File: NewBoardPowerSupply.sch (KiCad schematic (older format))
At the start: 22 parts, among them IC1 ADM7172ACPZ-4.2-R7, IC2 LT1716CS5#TRPBF, IC3 ADM7154ARDZ-3.3-R7, IC4 IRF9358PBF, U3 LM4040EIM3X-2.5_NOPB

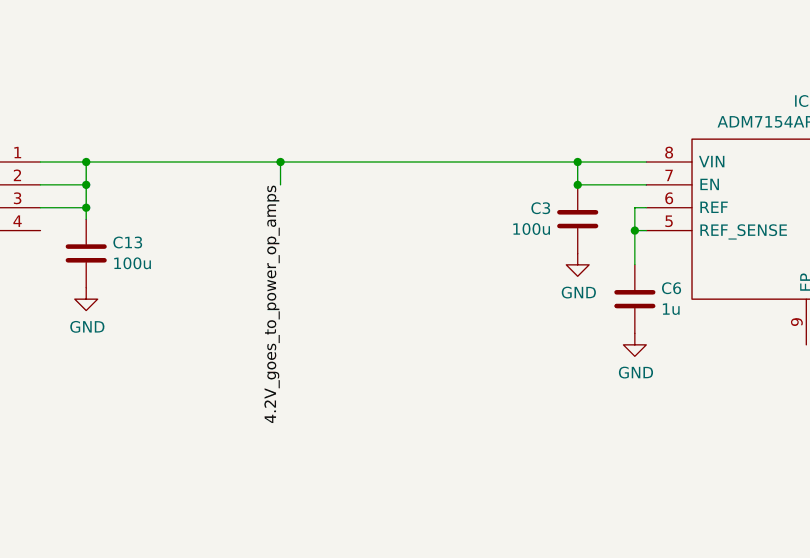
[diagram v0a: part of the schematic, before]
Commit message: added 4.2V port from pwr supply to pwr op amps sheet
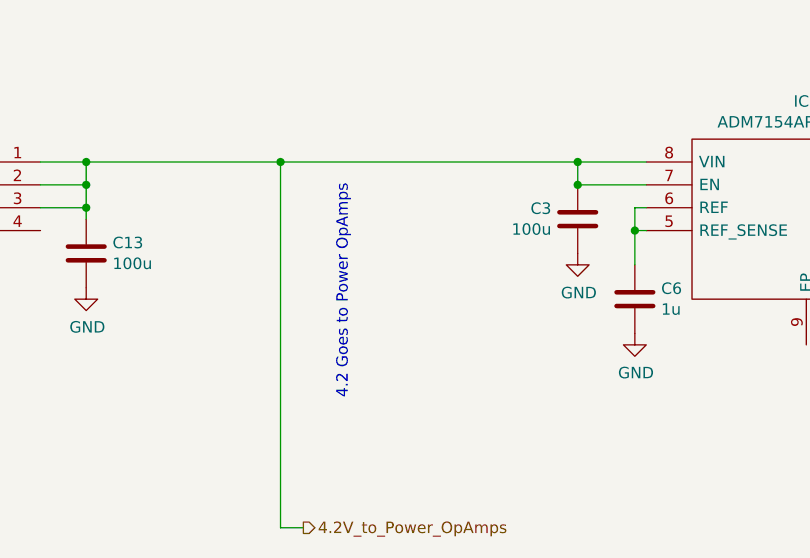
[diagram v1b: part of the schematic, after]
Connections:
- net 4.2V_goes_to_power_op_amps renamed 4.2V_to_Power_OpAmps
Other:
- note added: "4.2 Goes to Power OpAmps"
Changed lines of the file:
@@
 Text Label 8900 5500 0    50   ~ 0
 3.3V_rail
-Wire Wire Line
-	4650 5500 4650 5400
 Connection ~ 4650 5400
 Wire Wire Line
 	4650 5400 3800 5400
-Text Label 4650 5500 3    50   ~ 0
-4.2V_goes_to_power_op_amps
 Connection ~ 7600 2500
 Wire Wire Line
@@
 	7800 2100 7800 2500
 Connection ~ 6100 1000
+Text Notes 4950 5500 3    50   ~ 0
+4.2 Goes to Power OpAmps
+Text HLabel 4750 7000 2    50   Output ~ 0
+4.2V_to_Power_OpAmps
+Wire Wire Line
+	4650 7000 4750 7000
+Wire Wire Line
+	4650 5400 4650 7000
 $EndSCHEMATC

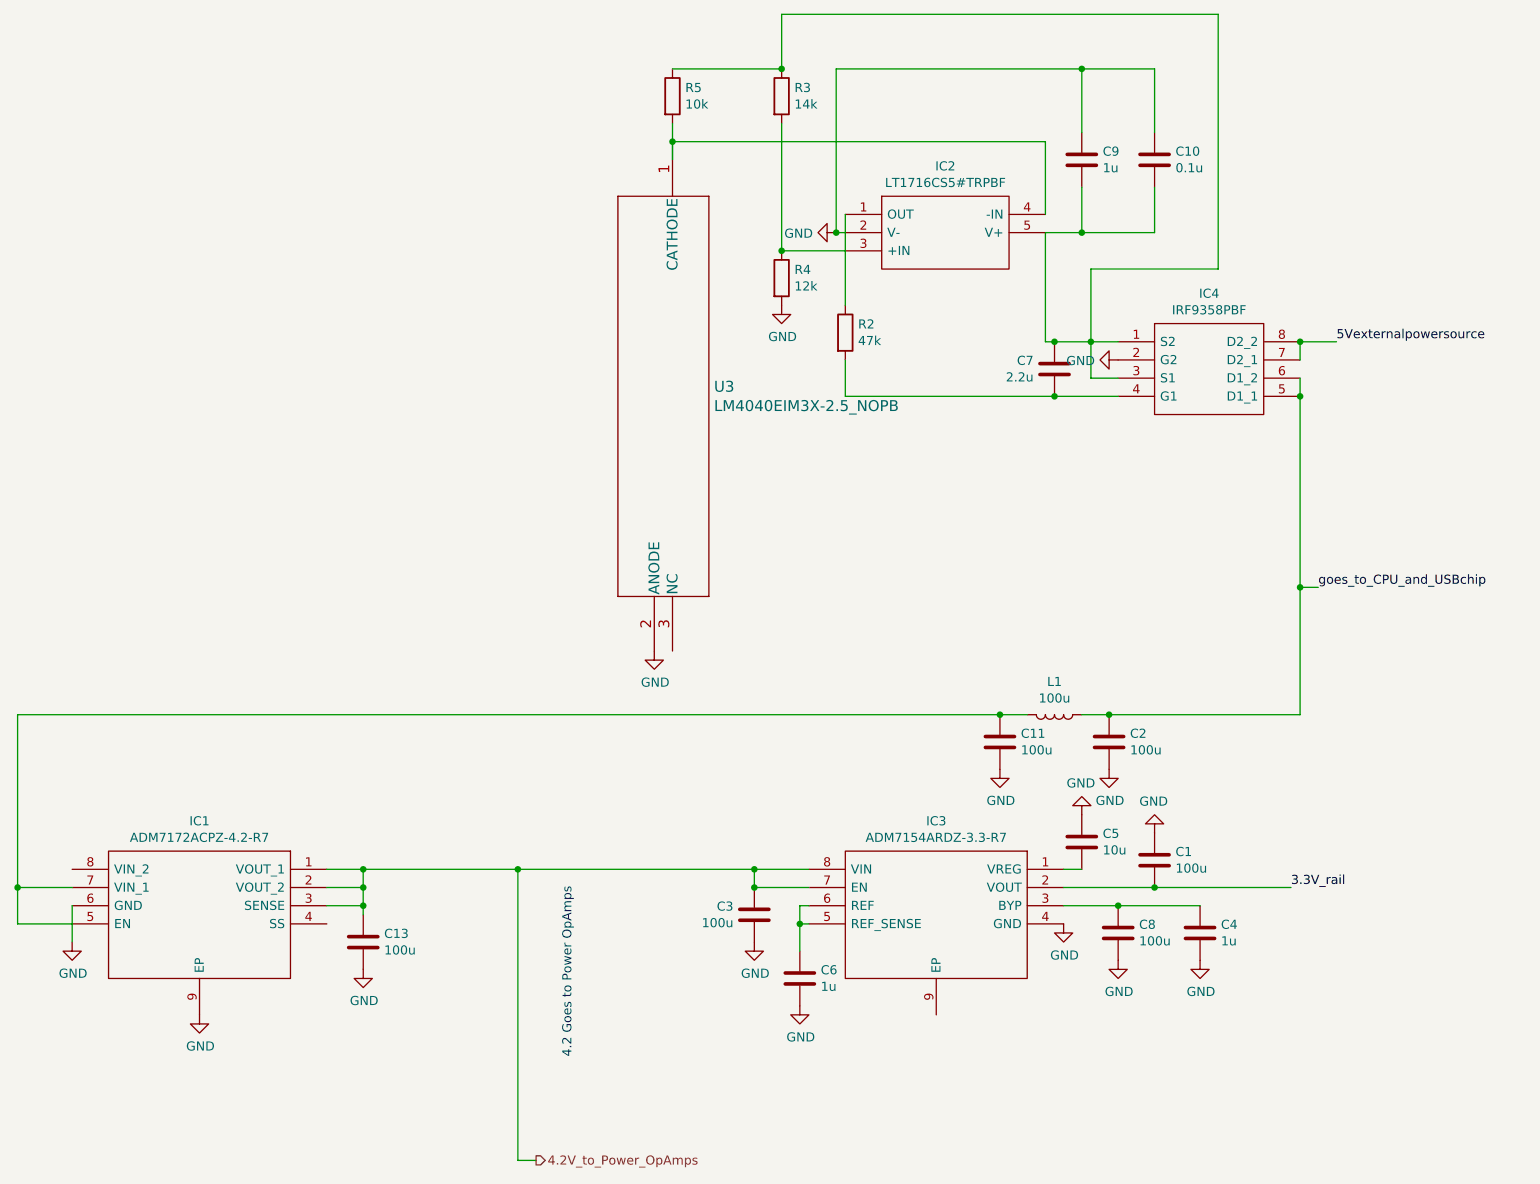
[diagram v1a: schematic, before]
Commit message: annotate all sheets
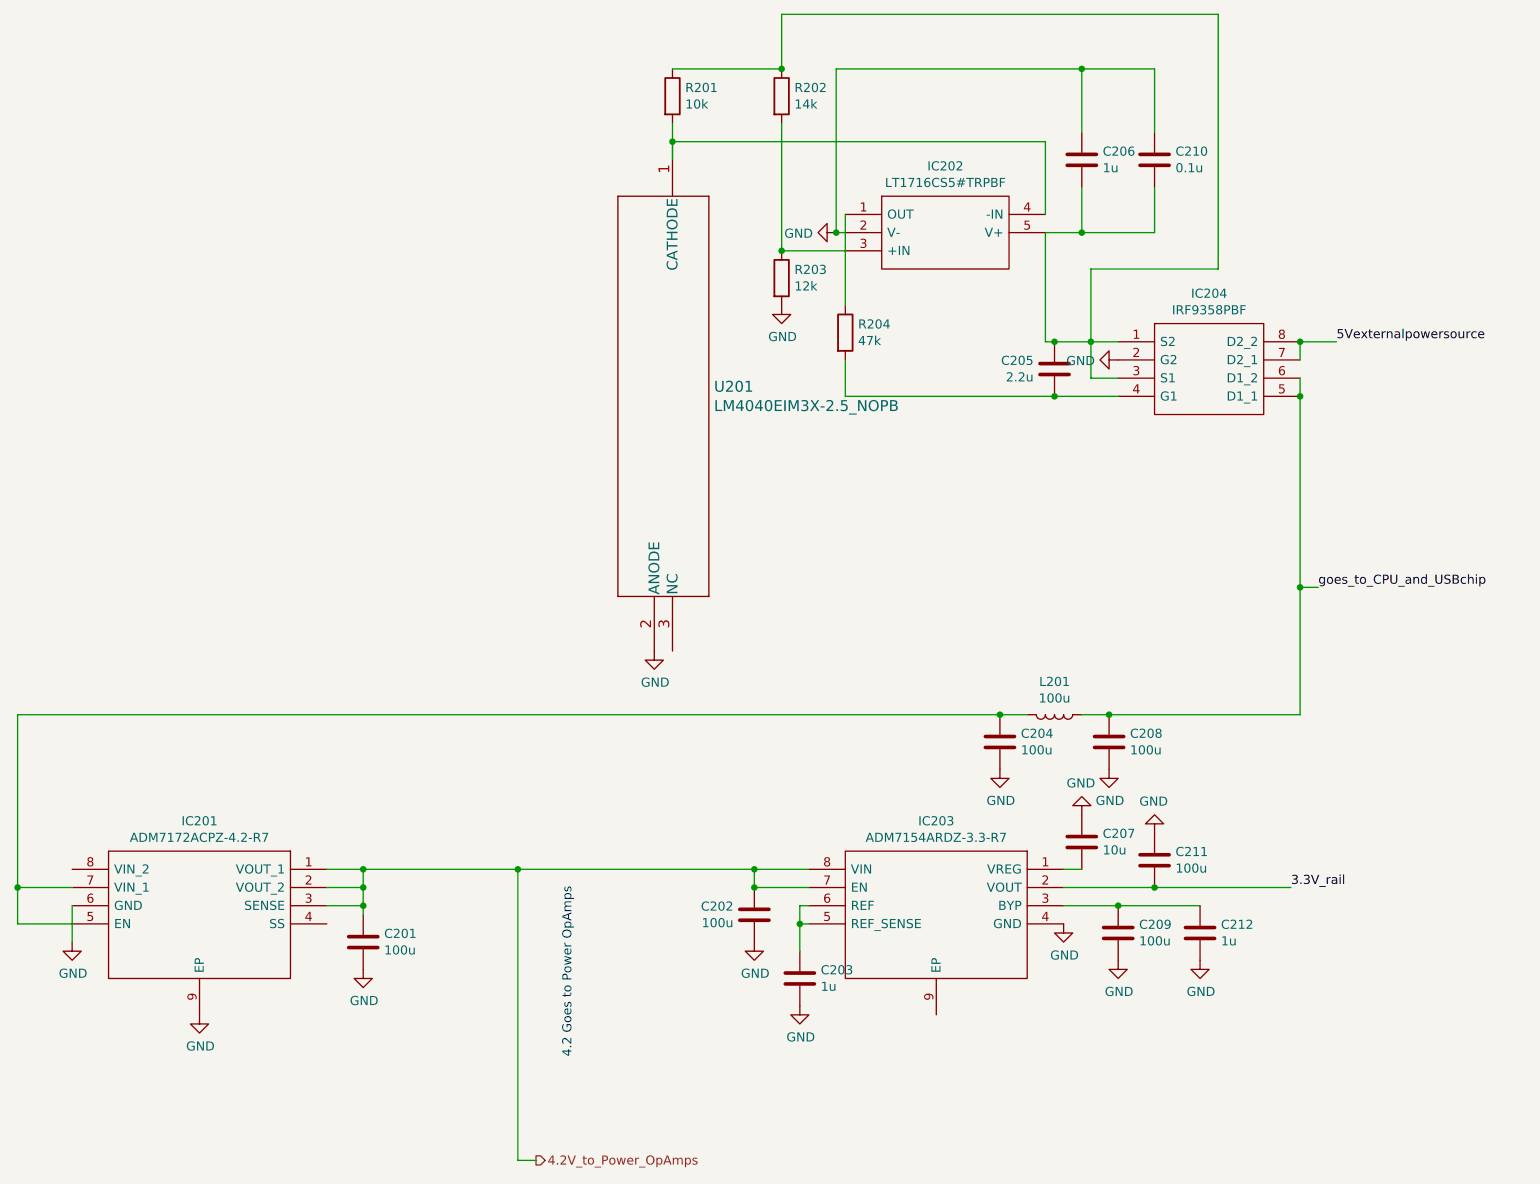
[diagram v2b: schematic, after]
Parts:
- renumbered C13 to C201, C3 to C202, C6 to C203, C11 to C204, C7 to C205, C9 to C206, C5 to C207, C2 to C208, C8 to C209, C10 to C210, C1 to C211, C4 to C212, IC1 to IC201, IC2 to IC202, IC3 to IC203, IC4 to IC204, L1 to L201, R5 to R201, R3 to R202, R4 to R203, R2 to R204, U3 to U201
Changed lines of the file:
@@
 $EndDescr
 $Comp
-L ADM7172ACPZ-4.2-R7:ADM7172ACPZ-4.2-R7 IC1
+L ADM7172ACPZ-4.2-R7:ADM7172ACPZ-4.2-R7 IC201
 U 1 1 60C1104B
 P 3600 5400
-F 0 "IC1" H 4300 5665 50  0000 C CNN
+F 0 "IC201" H 4300 5665 50  0000 C CNN
 F 1 "ADM7172ACPZ-4.2-R7" H 4300 5574 50  0000 C CNN
 F 2 "SON50P300X300X80-9N-D" H 4850 5500 50  0001 L CNN
@@
 $EndComp
 $Comp
-L Device:C C13
+L Device:C C201
 U 1 1 60C1975B
 P 3800 5800
-F 0 "C13" H 3915 5846 50  0000 L CNN
+F 0 "C201" H 3915 5846 50  0000 L CNN
 F 1 "100u" H 3915 5755 50  0000 L CNN
 F 2 "" H 3838 5650 50  0001 C CNN
@@
 $EndComp
 $Comp
-L power:GND #PWR01
+L power:GND #PWR0202
 U 1 1 60C1A400
 P 2900 6200
-F 0 "#PWR01" H 2900 5950 50  0001 C CNN
+F 0 "#PWR0202" H 2900 5950 50  0001 C CNN
 F 1 "GND" H 2905 6027 50  0000 C CNN
 F 2 "" H 2900 6200 50  0001 C CNN
@@
 $EndComp
 $Comp
-L power:GND #PWR02
+L power:GND #PWR0203
 U 1 1 60C1ADE2
 P 3800 5950
-F 0 "#PWR02" H 3800 5700 50  0001 C CNN
+F 0 "#PWR0203" H 3800 5700 50  0001 C CNN
 F 1 "GND" H 3805 5777 50  0000 C CNN
 F 2 "" H 3800 5950 50  0001 C CNN
@@
 $EndComp
 $Comp
-L ADM7154ARDZ-3.3-R7:ADM7154ARDZ-3.3-R7 IC3
+L ADM7154ARDZ-3.3-R7:ADM7154ARDZ-3.3-R7 IC203
 U 1 1 60C11888
 P 7650 5400
-F 0 "IC3" H 8350 5665 50  0000 C CNN
+F 0 "IC203" H 8350 5665 50  0000 C CNN
 F 1 "ADM7154ARDZ-3.3-R7" H 8350 5574 50  0000 C CNN
 F 2 "SOIC127P600X175-9N" H 8900 5500 50  0001 L CNN
@@
 $EndComp
 $Comp
-L Device:C C3
+L Device:C C202
 U 1 1 60C28A84
 P 5950 5650
-F 0 "C3" H 6065 5696 50  0000 L CNN
+F 0 "C202" H 6065 5696 50  0000 L CNN
 F 1 "100u" H 6065 5605 50  0000 L CNN
 F 2 "" H 5988 5500 50  0001 C CNN
@@
 $EndComp
 $Comp
-L Device:C C4
+L Device:C C212
 U 1 1 60C2CB1A
 P 8400 5750
-F 0 "C4" H 8515 5796 50  0000 L CNN
+F 0 "C212" H 8515 5796 50  0000 L CNN
 F 1 "1u" H 8515 5705 50  0000 L CNN
 F 2 "" H 8438 5600 50  0001 C CNN
@@
 $EndComp
 $Comp
-L Device:C C8
+L Device:C C209
 U 1 1 60C2E0AC
 P 7950 5750
-F 0 "C8" H 8065 5796 50  0000 L CNN
+F 0 "C209" H 8065 5796 50  0000 L CNN
 F 1 "100u" H 8065 5705 50  0000 L CNN
 F 2 "" H 7988 5600 50  0001 C CNN
@@
 $EndComp
 $Comp
-L power:GND #PWR015
+L power:GND #PWR0216
 U 1 1 60C305D6
 P 8400 5900
-F 0 "#PWR015" H 8400 5650 50  0001 C CNN
+F 0 "#PWR0216" H 8400 5650 50  0001 C CNN
 F 1 "GND" H 8405 5727 50  0000 C CNN
 F 2 "" H 8400 5900 50  0001 C CNN
@@
 $EndComp
 $Comp
-L power:GND #PWR013
+L power:GND #PWR0214
 U 1 1 60C30DEB
 P 7950 5900
-F 0 "#PWR013" H 7950 5650 50  0001 C CNN
+F 0 "#PWR0214" H 7950 5650 50  0001 C CNN
 F 1 "GND" H 7955 5727 50  0000 C CNN
 F 2 "" H 7950 5900 50  0001 C CNN
@@
 	6250 5500 5950 5500
 $Comp
-L power:GND #PWR04
+L power:GND #PWR0205
 U 1 1 60C319E0
 P 5950 5800
-F 0 "#PWR04" H 5950 5550 50  0001 C CNN
+F 0 "#PWR0205" H 5950 5550 50  0001 C CNN
 F 1 "GND" H 5955 5627 50  0000 C CNN
 F 2 "" H 5950 5800 50  0001 C CNN
@@
 $EndComp
 $Comp
-L Device:C C5
+L Device:C C207
 U 1 1 60C31F44
 P 7750 5250
-F 0 "C5" H 7865 5296 50  0000 L CNN
+F 0 "C207" H 7865 5296 50  0000 L CNN
 F 1 "10u" H 7865 5205 50  0000 L CNN
 F 2 "" H 7788 5100 50  0001 C CNN
@@
 	7650 5400 7750 5400
 $Comp
-L power:GND #PWR010
+L power:GND #PWR0211
 U 1 1 60C366F1
 P 7750 5100
-F 0 "#PWR010" H 7750 4850 50  0001 C CNN
+F 0 "#PWR0211" H 7750 4850 50  0001 C CNN
 F 1 "GND" H 7755 4927 50  0000 C CNN
 F 2 "" H 7750 5100 50  0001 C CNN
@@
 Connection ~ 5950 5500
 $Comp
-L Device:C C6
+L Device:C C203
 U 1 1 60C3804B
 P 6200 6000
-F 0 "C6" H 6315 6046 50  0000 L CNN
+F 0 "C203" H 6315 6046 50  0000 L CNN
 F 1 "1u" H 6315 5955 50  0000 L CNN
 F 2 "" H 6238 5850 50  0001 C CNN
@@
 	6200 5700 6200 5850
 $Comp
-L power:GND #PWR06
+L power:GND #PWR0207
 U 1 1 60C392F3
 P 6200 6150
-F 0 "#PWR06" H 6200 5900 50  0001 C CNN
+F 0 "#PWR0207" H 6200 5900 50  0001 C CNN
 F 1 "GND" H 6205 5977 50  0000 C CNN
 F 2 "" H 6200 6150 50  0001 C CNN
@@
 $EndComp
 $Comp
-L Device:C C1
+L Device:C C211
 U 1 1 60C39B45
 P 8150 5350
-F 0 "C1" H 8265 5396 50  0000 L CNN
+F 0 "C211" H 8265 5396 50  0000 L CNN
 F 1 "100u" H 8265 5305 50  0000 L CNN
 F 2 "" H 8188 5200 50  0001 C CNN
@@
 	7650 5500 8150 5500
 $Comp
-L power:GND #PWR014
+L power:GND #PWR0215
 U 1 1 60C3BD4C
 P 8150 5200
-F 0 "#PWR014" H 8150 4950 50  0001 C CNN
+F 0 "#PWR0215" H 8150 4950 50  0001 C CNN
 F 1 "GND" H 8155 5027 50  0000 C CNN
 F 2 "" H 8150 5200 50  0001 C CNN
@@
 	1900 5500 2200 5500
 $Comp
-L Device:C C11
+L Device:C C204
 U 1 1 60C3DCA3
 P 7300 4700
-F 0 "C11" H 7185 4654 50  0000 R CNN
+F 0 "C204" H 7185 4654 50  0000 R CNN
 F 1 "100u" H 7185 4745 50  0000 R CNN
 F 2 "" H 7338 4550 50  0001 C CNN
@@
 $EndComp
 $Comp
-L Device:L L1
+L Device:L L201
 U 1 1 60C3F9A3
 P 7600 4550
-F 0 "L1" V 7419 4550 50  0000 C CNN
+F 0 "L201" V 7419 4550 50  0000 C CNN
 F 1 "100u" V 7510 4550 50  0000 C CNN
 F 2 "" H 7600 4550 50  0001 C CNN
@@
 $EndComp
 $Comp
-L power:GND #PWR08
+L power:GND #PWR0209
 U 1 1 60C42E03
 P 7300 4850
-F 0 "#PWR08" H 7300 4600 50  0001 C CNN
+F 0 "#PWR0209" H 7300 4600 50  0001 C CNN
 F 1 "GND" H 7305 4677 50  0000 C CNN
 F 2 "" H 7300 4850 50  0001 C CNN
@@
 $EndComp
 $Comp
-L power:GND #PWR011
+L power:GND #PWR0212
 U 1 1 60C43694
 P 7900 4850
-F 0 "#PWR011" H 7900 4600 50  0001 C CNN
+F 0 "#PWR0212" H 7900 4600 50  0001 C CNN
 F 1 "GND" H 7905 4677 50  0000 C CNN
 F 2 "" H 7900 4850 50  0001 C CNN
@@
 	1900 4550 1900 5500
 $Comp
-L power:GND #PWR09
+L power:GND #PWR0210
 U 1 1 60C19547
 P 7650 5700
-F 0 "#PWR09" H 7650 5450 50  0001 C CNN
+F 0 "#PWR0210" H 7650 5450 50  0001 C CNN
 F 1 "GND" H 7655 5527 50  0000 C CNN
 F 2 "" H 7650 5700 50  0001 C CNN
@@
 $EndComp
 $Comp
-L LM4040:LM4040EIM3X-2.5_NOPB U3
+L LM4040:LM4040EIM3X-2.5_NOPB U201
 U 1 1 60C1A8C3
 P 5500 1400
-F 0 "U3" V 6847 1628 60  0000 L CNN
+F 0 "U201" V 6847 1628 60  0000 L CNN
 F 1 "LM4040EIM3X-2.5_NOPB" V 6953 1628 60  0000 L CNN
 F 2 "DBZ3" H 6900 1640 60  0001 C CNN
@@
 $EndComp
 $Comp
-L power:GND #PWR03
+L power:GND #PWR0204
 U 1 1 60C2C342
 P 5400 4200
-F 0 "#PWR03" H 5400 3950 50  0001 C CNN
+F 0 "#PWR0204" H 5400 3950 50  0001 C CNN
 F 1 "GND" H 5405 4027 50  0000 C CNN
 F 2 "" H 5400 4200 50  0001 C CNN
@@
 $EndComp
 $Comp
-L Device:R R5
+L Device:R R201
 U 1 1 60C8514F
 P 5500 1150
-F 0 "R5" H 5570 1196 50  0000 L CNN
+F 0 "R201" H 5570 1196 50  0000 L CNN
 F 1 "10k" H 5570 1105 50  0000 L CNN
 F 2 "" V 5430 1150 50  0001 C CNN
@@
 	5500 1000 6100 1000
 $Comp
-L Device:R R3
+L Device:R R202
 U 1 1 60C8D17C
 P 6100 1150
-F 0 "R3" H 6170 1196 50  0000 L CNN
+F 0 "R202" H 6170 1196 50  0000 L CNN
 F 1 "14k" H 6170 1105 50  0000 L CNN
 F 2 "" V 6030 1150 50  0001 C CNN
@@
 $EndComp
 $Comp
-L power:GND #PWR07
+L power:GND #PWR0208
 U 1 1 60C7B138
 P 6400 1900
-F 0 "#PWR07" H 6400 1650 50  0001 C CNN
+F 0 "#PWR0208" H 6400 1650 50  0001 C CNN
 F 1 "GND" V 6405 1772 50  0000 R CNN
 F 2 "" H 6400 1900 50  0001 C CNN
@@
 $EndComp
 $Comp
-L LT1716CS5#TRPBF:LT1716CS5#TRPBF IC2
+L LT1716CS5#TRPBF:LT1716CS5#TRPBF IC202
 U 1 1 60C4116D
 P 6450 1800
-F 0 "IC2" H 7000 2065 50  0000 C CNN
+F 0 "IC202" H 7000 2065 50  0000 C CNN
 F 1 "LT1716CS5#TRPBF" H 7000 1974 50  0000 C CNN
 F 2 "SOT95P280X100-5N" H 7400 1900 50  0001 L CNN
@@
 	6100 2000 6450 2000
 $Comp
-L Device:R R4
+L Device:R R203
 U 1 1 60C99B19
 P 6100 2150
-F 0 "R4" H 6170 2196 50  0000 L CNN
+F 0 "R203" H 6170 2196 50  0000 L CNN
 F 1 "12k" H 6170 2105 50  0000 L CNN
 F 2 "" V 6030 2150 50  0001 C CNN
@@
 Connection ~ 6100 2000
 $Comp
-L power:GND #PWR05
+L power:GND #PWR0206
 U 1 1 60C9A55D
 P 6100 2300
-F 0 "#PWR05" H 6100 2050 50  0001 C CNN
+F 0 "#PWR0206" H 6100 2050 50  0001 C CNN
 F 1 "GND" H 6105 2127 50  0000 C CNN
 F 2 "" H 6100 2300 50  0001 C CNN
@@
 Connection ~ 7750 1900
 $Comp
-L Device:C C9
+L Device:C C206
 U 1 1 60CA03AF
 P 7750 1500
-F 0 "C9" H 7865 1546 50  0000 L CNN
+F 0 "C206" H 7865 1546 50  0000 L CNN
 F 1 "1u" H 7865 1455 50  0000 L CNN
 F 2 "" H 7788 1350 50  0001 C CNN
@@
 	7750 1350 7750 1000
 $Comp
-L Device:C C10
+L Device:C C210
 U 1 1 60CA132A
 P 8150 1500
-F 0 "C10" H 8265 1546 50  0000 L CNN
+F 0 "C210" H 8265 1546 50  0000 L CNN
 F 1 "0.1u" H 8265 1455 50  0000 L CNN
 F 2 "" H 8188 1350 50  0001 C CNN
@@
 Connection ~ 6400 1900
 $Comp
-L Device:C C7
+L Device:C C205
 U 1 1 60CA63E5
 P 7600 2650
-F 0 "C7" H 7715 2696 50  0000 L CNN
+F 0 "C205" H 7715 2696 50  0000 L CNN
 F 1 "2.2u" H 7715 2605 50  0000 L CNN
 F 2 "" H 7638 2500 50  0001 C CNN
@@
 	7550 1900 7550 2500
 $Comp
-L IRF9358PBF:IRF9358PBF IC4
+L IRF9358PBF:IRF9358PBF IC204
 U 1 1 60C1CFE4
 P 7950 2500
-F 0 "IC4" H 8450 2765 50  0000 C CNN
+F 0 "IC204" H 8450 2765 50  0000 C CNN
 F 1 "IRF9358PBF" H 8450 2674 50  0000 C CNN
 F 2 "SOIC127P600X175-8N" H 8800 2600 50  0001 L CNN
@@
 	7950 2700 7800 2700
 $Comp
-L power:GND #PWR012
+L power:GND #PWR0213
 U 1 1 60CBDBBD
 P 7950 2600
-F 0 "#PWR012" H 7950 2350 50  0001 C CNN
+F 0 "#PWR0213" H 7950 2350 50  0001 C CNN
 F 1 "GND" V 7955 2472 50  0000 R CNN
 F 2 "" H 7950 2600 50  0001 C CNN
@@
 	7800 2500 7950 2500
 $Comp
-L Device:R R2
+L Device:R R204
 U 1 1 60CC5789
 P 6450 2450
-F 0 "R2" H 6520 2496 50  0000 L CNN
+F 0 "R204" H 6520 2496 50  0000 L CNN
 F 1 "47k" H 6520 2405 50  0000 L CNN
 F 2 "" V 6380 2450 50  0001 C CNN
@@
 	6450 1800 6450 2300
 $Comp
-L Device:C C2
+L Device:C C208
 U 1 1 60C41D63
 P 7900 4700
-F 0 "C2" H 7785 4654 50  0000 R CNN
+F 0 "C208" H 7785 4654 50  0000 R CNN
 F 1 "100u" H 7785 4745 50  0000 R CNN
 F 2 "" H 7938 4550 50  0001 C CNN
@@
 $EndComp
 $Comp
-L power:GND #PWR016
+L power:GND #PWR0201
 U 1 1 60C8805A
 P 2200 5800
-F 0 "#PWR016" H 2200 5550 50  0001 C CNN
+F 0 "#PWR0201" H 2200 5550 50  0001 C CNN
 F 1 "GND" H 2205 5627 50  0000 C CNN
 F 2 "" H 2200 5800 50  0001 C CNN

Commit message: add footprints julia
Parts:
- IC201: footprint SON50P300X300X80-9N-D -> footprint libraries:ADM7172ACPZ-4.2-R7
- IC202: footprint SOT95P280X100-5N -> footprint libraries:LT1716CS5#TRPBF
- IC203: footprint SOIC127P600X175-9N -> footprint libraries:ADA4528-2ACPZ-RL
- U201: footprint DBZ3 -> footprint libraries:LM4040EIM3X-2.5&slash_NOPB
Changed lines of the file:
@@
 F 0 "IC201" H 4300 5665 50  0000 C CNN
 F 1 "ADM7172ACPZ-4.2-R7" H 4300 5574 50  0000 C CNN
-F 2 "SON50P300X300X80-9N-D" H 4850 5500 50  0001 L CNN
+F 2 "footprint libraries:ADM7172ACPZ-4.2-R7" H 4850 5500 50  0001 L CNN
 F 3 "https://www.analog.com/media/en/technical-documentation/data-sheets/ADM7172.pdf" H 4850 5400 50  0001 L CNN
 F 4 "LDO Voltage Regulators 2A Hi PSRR FT L DO 4.2Vo" H 4850 5300 50  0001 L CNN "Description"
@@
 F 0 "IC203" H 8350 5665 50  0000 C CNN
 F 1 "ADM7154ARDZ-3.3-R7" H 8350 5574 50  0000 C CNN
-F 2 "SOIC127P600X175-9N" H 8900 5500 50  0001 L CNN
+F 2 "footprint libraries:ADA4528-2ACPZ-RL" H 8900 5500 50  0001 L CNN
 F 3 "http://www.analog.com/media/en/technical-documentation/data-sheets/ADM7154.pdf" H 8900 5400 50  0001 L CNN
 F 4 "ANALOG DEVICES - ADM7154ARDZ-3.3-R7 - LDO, FIXED, 3.3V, 0.6A, NSOIC-8" H 8900 5300 50  0001 L CNN "Description"
@@
 F 0 "U201" V 6847 1628 60  0000 L CNN
 F 1 "LM4040EIM3X-2.5_NOPB" V 6953 1628 60  0000 L CNN
-F 2 "DBZ3" H 6900 1640 60  0001 C CNN
+F 2 "footprint libraries:LM4040EIM3X-2.5&slash_NOPB" H 6900 1640 60  0001 C CNN
 F 3 "" H 5500 1400 60  0000 C CNN
 	1    5500 1400
@@
 F 0 "IC202" H 7000 2065 50  0000 C CNN
 F 1 "LT1716CS5#TRPBF" H 7000 1974 50  0000 C CNN
-F 2 "SOT95P280X100-5N" H 7400 1900 50  0001 L CNN
+F 2 "footprint libraries:LT1716CS5#TRPBF" H 7400 1900 50  0001 L CNN
 F 3 "https://www.analog.com/media/en/technical-documentation/data-sheets/LT1716.pdf" H 7400 1800 50  0001 L CNN
 F 4 "Analog Comparators SOT-23, 44V, Over-The-Top, uP, Prec R2R" H 7400 1700 50  0001 L CNN "Description"

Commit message: assigned irf footprint
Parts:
- IC204: footprint SOIC127P600X175-8N -> footprint libraries:IRF9358PBF
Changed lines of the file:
@@
 F 0 "IC204" H 8450 2765 50  0000 C CNN
 F 1 "IRF9358PBF" H 8450 2674 50  0000 C CNN
-F 2 "SOIC127P600X175-8N" H 8800 2600 50  0001 L CNN
+F 2 "footprint libraries:IRF9358PBF" H 8800 2600 50  0001 L CNN
 F 3 "https://www.infineon.com/dgdl/irf9358pbf.pdf?fileId=5546d462533600a4015356114ffa1da5" H 8800 2500 50  0001 L CNN
 F 4 "International Rectifier IRF9358PBF Dual P-channel MOSFET Transistor, 9.2 A, -30 V, 8-Pin SOIC" H 8800 2400 50  0001 L CNN "Description"
